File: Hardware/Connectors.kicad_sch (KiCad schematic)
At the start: 26 parts, among them J1 SMA_Edge, J3 USB_C_Receptacle, J4 SMA_Edge, J5 JST_Locking_6, U3 LMV7219M5

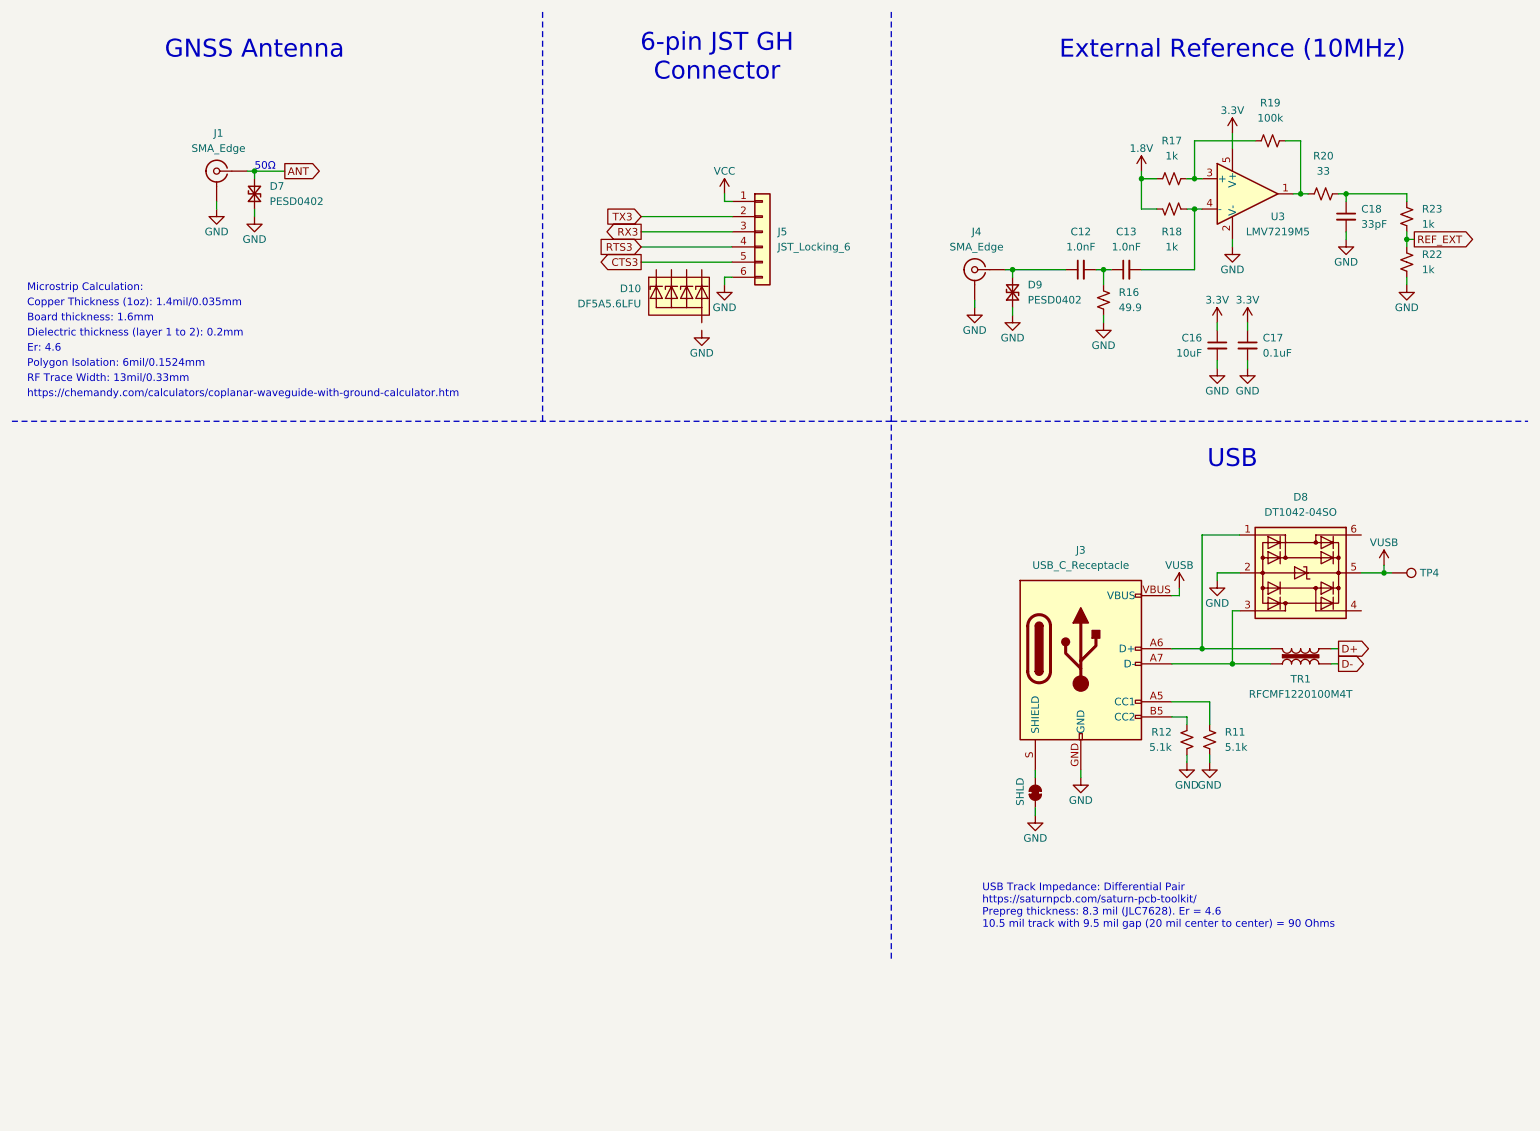
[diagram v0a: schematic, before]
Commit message: Ready for airwire review
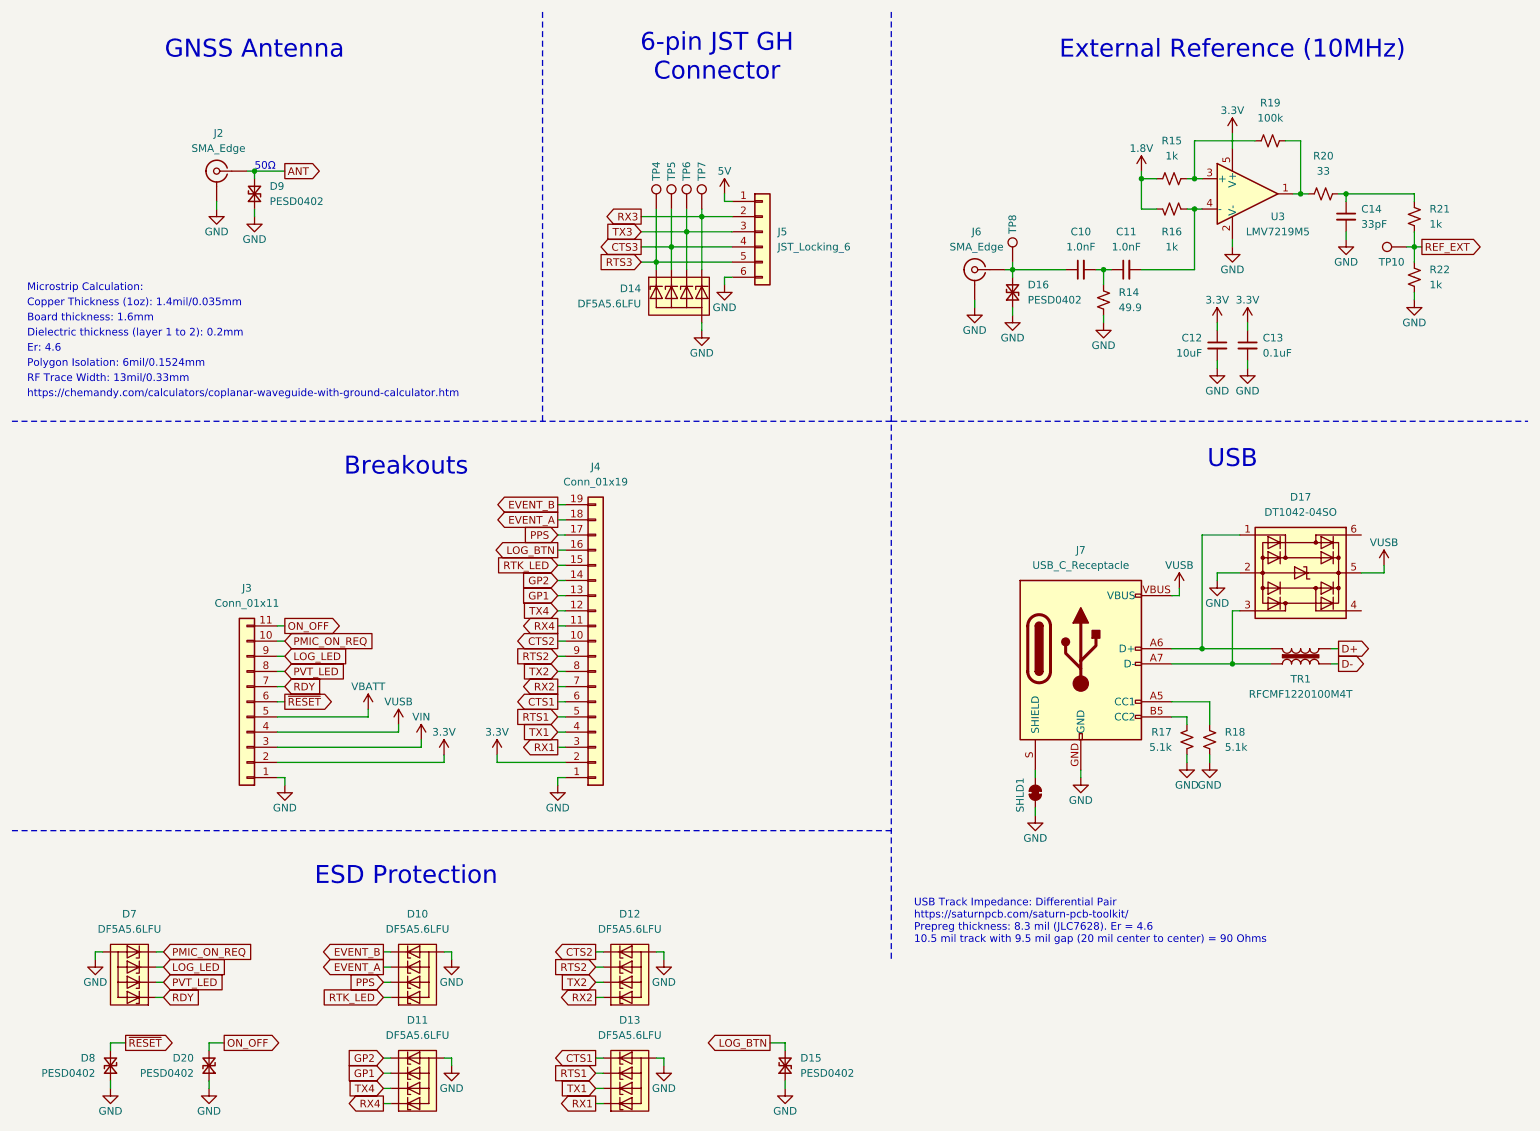
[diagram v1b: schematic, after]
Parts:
- added D10, D11, D12, D13, D7: DF5A5.6LFU, SparkFun-Semiconductor-Standard:SOT-353, symbol SparkFun-DiscreteSemi:D_TVS_ESD_4_HS
- added D15, D20, D8: PESD0402, SparkFun-Capacitor:C_0402_1005Metric, symbol SparkFun-DiscreteSemi:D_TVS_0402
- added J3: Conn_01x11, SparkFun-Connector:1x11, symbol SparkFun-Connector:Conn_01x11
- added J4: Conn_01x19, SparkFun-Connector:1x19, symbol SparkFun-Connector:Conn_01x19
- added TP10, TP5, TP6, TP7, TP8: 1.25mm, SparkFun-Connector:TestPoint-1.25mm, symbol SparkFun-Connector:TestPoint_1.25mm
- renumbered C12 to C10, C13 to C11, C16 to C12, C17 to C13, C18 to C14, D10 to D14, D9 to D16, D8 to D17, D7 to D9, J1 to J2, J4 to J6, J3 to J7, R16 to R14, R17 to R15, R18 to R16, R12 to R17, R11 to R18, R23 to R21, SHLD to SHLD1
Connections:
- net 3.3V: now also J3.2 (Pin_2), J4.2 (Pin_2)
- net CTS3: now also D14.3 (K2), J5.4 (Pin_4), TP5.1; no longer J5.5 (Pin_5)
- net GND: now also D14.2 (A), D10.2 (A), D11.2 (A), D12.2 (A), D13.2 (A), D15.1 (A1), D20.1 (A1), D7.2 (A), D8.1 (A1), J3.1 (Pin_1), J4.1 (Pin_1)
- net REF_EXT: now also TP10.1
- net RTS3: now also D14.1 (K1), J5.5 (Pin_5), TP4.1; no longer J5.4 (Pin_4)
- net RX3: now also D14.5 (K4), J5.2 (Pin_2), TP7.1; no longer J5.3 (Pin_3)
- net TX3: now also D14.4 (K3), J5.3 (Pin_3), TP6.1; no longer J5.2 (Pin_2)
- net VUSB: now also J3.4 (Pin_4); no longer TP4.1
- net at C10.1, D16.2 (A2), J6.1 (In): now also TP8.1
- net VCC renamed 5V
- new net CTS1: D13.5 (K4), J4.6 (Pin_6)
- new net CTS2: D12.5 (K4), J4.10 (Pin_10)
- new net EVENT_A: D10.4 (K3), J4.18 (Pin_18)
- new net EVENT_B: D10.5 (K4), J4.19 (Pin_19)
- new net GP1: D11.4 (K3), J4.13 (Pin_13)
- new net GP2: D11.5 (K4), J4.14 (Pin_14)
- new net LOG_BTN: D15.2 (A2), J4.16 (Pin_16)
- new net LOG_LED: D7.4 (K3), J3.9 (Pin_9)
- new net ON_OFF: D20.2 (A2), J3.11 (Pin_11)
- new net PMIC_ON_REQ: D7.5 (K4), J3.10 (Pin_10)
- new net PPS: D10.3 (K2), J4.17 (Pin_17)
- new net PVT_LED: D7.3 (K2), J3.8 (Pin_8)
- new net RDY: D7.1 (K1), J3.7 (Pin_7)
- new net RTK_LED: D10.1 (K1), J4.15 (Pin_15)
- new net RTS1: D13.4 (K3), J4.5 (Pin_5)
- new net RTS2: D12.4 (K3), J4.9 (Pin_9)
- new net RX1: D13.1 (K1), J4.3 (Pin_3)
- new net RX2: D12.1 (K1), J4.7 (Pin_7)
- new net RX4: D11.1 (K1), J4.11 (Pin_11)
- new net TX1: D13.3 (K2), J4.4 (Pin_4)
- new net TX2: D12.3 (K2), J4.8 (Pin_8)
- new net TX4: D11.3 (K2), J4.12 (Pin_12)
- new net VBATT: J3.5 (Pin_5)
- new net VIN: J3.3 (Pin_3)
- new net ~{RESET}: D8.2 (A2), J3.6 (Pin_6)
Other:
- note added: "Breakouts"
- note added: "ESD Protection"
- moved on the sheet: R21, R22

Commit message: Routing - WIP
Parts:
- removed D15, D20, D8: PESD0402, SparkFun-Capacitor:C_0402_1005Metric, symbol SparkFun-DiscreteSemi:D_TVS_0402
- added D15, D8: DF5A5.6LFU, SparkFun-Semiconductor-Standard:SOT-353, symbol SparkFun-DiscreteSemi:D_TVS_ESD_4_HS
- added TP12, TP9: 1.25mm, SparkFun-Connector:TestPoint-1.25mm, symbol SparkFun-Connector:TestPoint_1.25mm
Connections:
- net CTS1: now also D13.4 (K3); no longer D13.5 (K4)
- net CTS2: now also D12.4 (K3); no longer D12.5 (K4)
- net EVENT_A: now also D15.1 (K1), D15.5 (K4); no longer D10.4 (K3)
- net EVENT_B: now also D15.3 (K2), D15.4 (K3); no longer D10.5 (K4)
- net GND: now also D15.2 (A), D8.2 (A)
- net GP1: now also D11.3 (K2); no longer D11.4 (K3)
- net GP2: now also D11.4 (K3); no longer D11.5 (K4)
- net LOG_BTN: now also D10.1 (K1)
- net LOG_LED: now also D7.3 (K2); no longer D7.4 (K3)
- net ON_OFF: now also D8.3 (K2), D8.4 (K3)
- net PMIC_ON_REQ: now also D8.1 (K1), D8.5 (K4); no longer D7.5 (K4)
- net PVT_LED: now also D7.4 (K3); no longer D7.3 (K2)
- net RDY: now also D7.5 (K4); no longer D7.1 (K1)
- net RTK_LED: now also D10.5 (K4); no longer D10.1 (K1)
- net RTS1: now also D13.3 (K2); no longer D13.4 (K3)
- net RTS2: now also D12.3 (K2); no longer D12.4 (K3)
- net RTS3: now also D14.4 (K3); no longer D14.1 (K1)
- net RX1: now also D13.5 (K4); no longer D13.1 (K1)
- net RX2: now also D12.5 (K4); no longer D12.1 (K1)
- net RX4: now also D11.5 (K4); no longer D11.1 (K1)
- net TX1: now also D13.1 (K1); no longer D13.3 (K2)
- net TX2: now also D12.1 (K1); no longer D12.3 (K2)
- net TX3: now also D14.1 (K1); no longer D14.4 (K3)
- net TX4: now also D11.1 (K1); no longer D11.3 (K2)
- net ~{RESET}: now also D7.1 (K1)
- net at J7.A7 (D-), J7.B7 (D-), TR1.1: now also D17.1 (I/O1), D17.6 (I/O4), TP12.1; no longer D17.3 (I/O2)
- net at J7.A6 (D+), J7.B6 (D+), TR1.3: now also D17.3 (I/O2), D17.4 (I/O3), TP9.1; no longer D17.1 (I/O1)
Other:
- note added: "RF Track Impedance: Coplanar Single Ended https://jlcpcb.com/pcb-impedance-calculator JLCPCB JLC0416H-7628, 4-layer, 1.59mm, 1oz outer, 0.5oz inner Prepreg: thickness: 8.28 mil (0.21mm), Er = 4.4 6 mil trace to copper (L1 ground pour isolation) 10.4 mil track = 50 Ohms"
- note added: "USB Track Impedance: Differential Pair https://jlcpcb.com/pcb-impedance-calculator JLCPCB JLC0416H-7628, 4-layer, 1.59mm, 1oz outer, 0.5oz inner Prepreg: thickness: 8.28 mil (0.21mm), Er = 4.4 6 mil trace to copper (L1 ground pour isolation) 10.7 mil track with 9.3 mil gap (20 mil center to center) = 90 Ohms"
- note removed: "Board thickness: 1.6mm"
- note removed: "Copper Thickness (1oz): 1.4mil/0.035mm"
- note removed: "Dielectric thickness (layer 1 to 2): 0.2mm"
- note removed: "Er: 4.6"
- note removed: "Microstrip Calculation:"
- note removed: "Polygon Isolation: 6mil/0.1524mm"
- note removed: "RF Trace Width: 13mil/0.33mm"
- note removed: "USB Track Impedance: Differential Pair https://saturnpcb.com/saturn-pcb-toolkit/ Prepreg thickness: 8.3 mil (JLC7628). Er = 4.6 10.5 mil track with 9.5 mil gap (20 mil center to center) = 90 Ohms"
- note removed: "https://chemandy.com/calculators/coplanar-waveguide-with-ground-calculator.htm"
- moved on the sheet: D10, D11, D12, D13, D17, D7, J7, R17, R18, SHLD1, TP4, TP6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

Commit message: Routed
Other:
- note added: "Microstrip (Coplanar Single Ended) 50Ω Calculation: https://jlcpcb.com/pcb-impedance-calculator Board thickness: 1.6mm. Layers: 4. Er: 4.4 (7628 Prepreg) Dielectric Thickness (Layer 1 to 2): 8.28mil/0.2104mm (JLC7628) Copper Thickness (1oz outer / 0.5oz inner): 1.38mil/0.035mm Polygon Isolation: 7mil/0.1778mm Trace Width: 11.1mil/0.2819mm"
- note added: "USB Track Impedance: Coplanar Differential Pair @ 90Ω https://jlcpcb.com/pcb-impedance-calculator Board Thickness: 1.6mm. Layers: 4. Er: 4.4 (7628 Prepreg) Dielectric Thickness (Layer 1 to 2): 8.28mil/0.21mm (JLC7628) Copper Thickness (1oz outer / 0.5oz inner): 1.38mil/0.035mm Polygon Isolation: 7mil/0.1778mm Trace Spacing: 9.07mil/0.2304mm Trace Width: 10.93mil/0.2776mm Trace center-to-center: 2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"
- note removed: "RF Track Impedance: Coplanar Single Ended https://jlcpcb.com/pcb-impedance-calculator JLCPCB JLC0416H-7628, 4-layer, 1.59mm, 1oz outer, 0.5oz inner Prepreg: thickness: 8.28 mil (0.21mm), Er = 4.4 6 mil trace to copper (L1 ground pour isolation) 10.4 mil track = 50 Ohms"
- note removed: "USB Track Impedance: Differential Pair https://jlcpcb.com/pcb-impedance-calculator JLCPCB JLC0416H-7628, 4-layer, 1.59mm, 1oz outer, 0.5oz inner Prepreg: thickness: 8.28 mil (0.21mm), Er = 4.4 6 mil trace to copper (L1 ground pour isolation) 10.7 mil track with 9.3 mil gap (20 mil center to center) = 90 Ohms"
- moved on the sheet: D17, J7, R17, R18, SHLD1, TP12, TP9, TR1

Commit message: Schematic updates after proto review
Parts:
- added VOUT1: ~, SparkFun-Jumper:Jumper_3_NC-1_Trace, symbol SparkFun-Jumper:SolderJumper_3_Bridged12
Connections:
- net 3.3V: now also VOUT1.3 (C)
- net 5V: now also VOUT1.1 (A); no longer J5.1 (Pin_1)
- net PPS: now also D10.4 (K3)
- new net: J5.1 (Pin_1), VOUT1.2 (B)
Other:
- note added: "External reference: Input impedance 50Ω Detection level: -14dBm Max supported level: +14dBm"
- note added: "JST Pin 1 is 5V by default. Change this jumper to select 3.3V."
- note added: "VBATT: 3.3V +/- 5% Open the VBATT jumper before connecting an external voltage."
- note added: "VIN: 5.0V +/- 10%"
- title: Connectors -> SparkFun GNSS mosaic-T - Connectors
- moved on the sheet: J3, J4

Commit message: More updates, post proto review
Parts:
- added TP13: 1.25mm, SparkFun-Connector:TestPoint-1.25mm, symbol SparkFun-Connector:TestPoint_1.25mm
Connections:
- net at J5.1 (Pin_1), VOUT1.2 (B): now also TP13.1
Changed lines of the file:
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@@
 	)
 	(junction
+		(at 132.08 40.64)
+		(diameter 0)
+		(color 0 0 0 0)
+	)
+	(junction
 		(at 201.93 40.64)
 		(diameter 0)
@@
 	(wire
 		(pts
+			(xy 132.08 40.64) (xy 132.08 44.45)
+		)
+		(stroke
+			(width 0)
+			(type default)
+		)
+	)
+	(wire
+		(pts
 			(xy 194.31 55.88) (xy 195.58 55.88)
 		)
@@
 	(wire
 		(pts
+			(xy 133.35 40.64) (xy 132.08 40.64)
+		)
+		(stroke
+			(width 0)
+			(type default)
+		)
+	)
+	(wire
+		(pts
 			(xy 231.14 120.65) (xy 232.41 120.65)
 		)
@@
 	(wire
 		(pts
-			(xy 132.08 38.1) (xy 132.08 44.45)
+			(xy 132.08 38.1) (xy 132.08 40.64)
 		)
 		(stroke
@@
 					(unit 1)
 				)
+			)
+		)
+	)
+	(symbol
+		(lib_id "SparkFun-Connector:TestPoint_1.25mm")
+		(at 133.35 40.64 270)
+		(unit 1)
+		(exclude_from_sim no)
+		(in_bom yes)
+		(on_board yes)
+		(dnp no)
+		(fields_autoplaced yes)
+		(property "Reference" "TP13"
+			(at 138.43 40.64 0)
+			(do_not_autoplace yes)
+			(effects
+				(font
+					(size 1.27 1.27)
+				)
+				(hide yes)
+			)
+		)
+		(property "Value" "1.25mm"
+			(at 129.54 40.64 0)
+			(effects
+				(font
+					(size 1.27 1.27)
+				)
+				(hide yes)
+			)
+		)
+		(property "Footprint" "SparkFun-Connector:TestPoint-1.25mm"
+			(at 127 40.64 0)
+			(effects
+				(font
+					(size 1.27 1.27)
+				)
+				(hide yes)
+			)
+		)
+		(property "Datasheet" "~"
+			(at 125.73 40.64 0)
+			(effects
+				(font
+					(size 1.27 1.27)
+				)
+				(hide yes)
+			)
+		)
+		(property "Description" "Test Point"
+			(at 123.19 40.64 0)
+			(effects
+				(font
+					(size 1.27 1.27)
+				)
+				(hide yes)
+			)
+		)
+		(pin "1"
+		)
+		(instances
+			(project "SparkFun_GNSS_mosaic-T"
+				(path "/e3dd3ae4-244d-4cba-9cca-5d2abf83f29a/31a2c60b-91be-4113-ae16-f797035e304d"
+					(reference "TP13")
+					(unit 1)
+				)
